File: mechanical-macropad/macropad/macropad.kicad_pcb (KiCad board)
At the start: 2 copper layers, 76 x 176.4 mm, 89 parts, among them J1 USB_B_Micro, J2 AVR-ISP-6, K1 KEYSW, K10 KEYSW, K11 KEYSW, K12 KEYSW, K13 KEYSW, K14 KEYSW, K15 KEYSW, K16 KEYSW, K17 KEYSW, K18 KEYSW, K19 KEYSW, K2 KEYSW, K20 KEYSW, K21 KEYSW, K22 KEYSW, K23 KEYSW, K24 KEYSW, K25 KEYSW, K26 KEYSW, K27 KEYSW, K28 KEYSW, K3 KEYSW, K4 KEYSW, K5 KEYSW, K6 KEYSW, K7 KEYSW, K8 KEYSW, K9 KEYSW, SW1 SW_Push, U1 ATMEGA32U4, X1 XTAL_GND

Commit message: Final cleanup
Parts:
- moved C6 0.59 mm to (175.2, 85.8)
- moved C14 0.28 mm to (159.7, 81.0)
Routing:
- net GND: track 27.7 -> 27.1 mm
- net /ISP_RESET: track 51.7 -> 51.2 mm
- added copper zone on B.Cu, net VCC

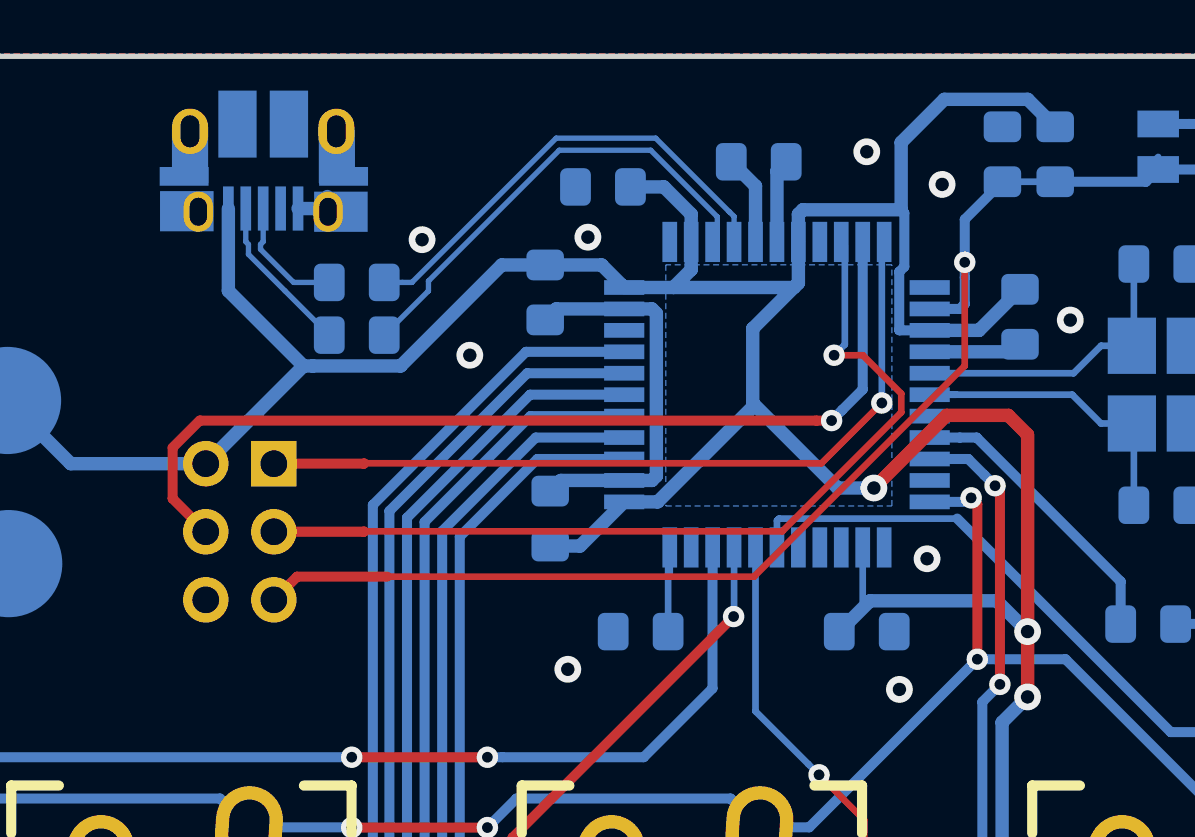
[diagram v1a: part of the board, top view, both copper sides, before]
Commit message: Add a beautiful VCC pour under the MCU to clean up traces
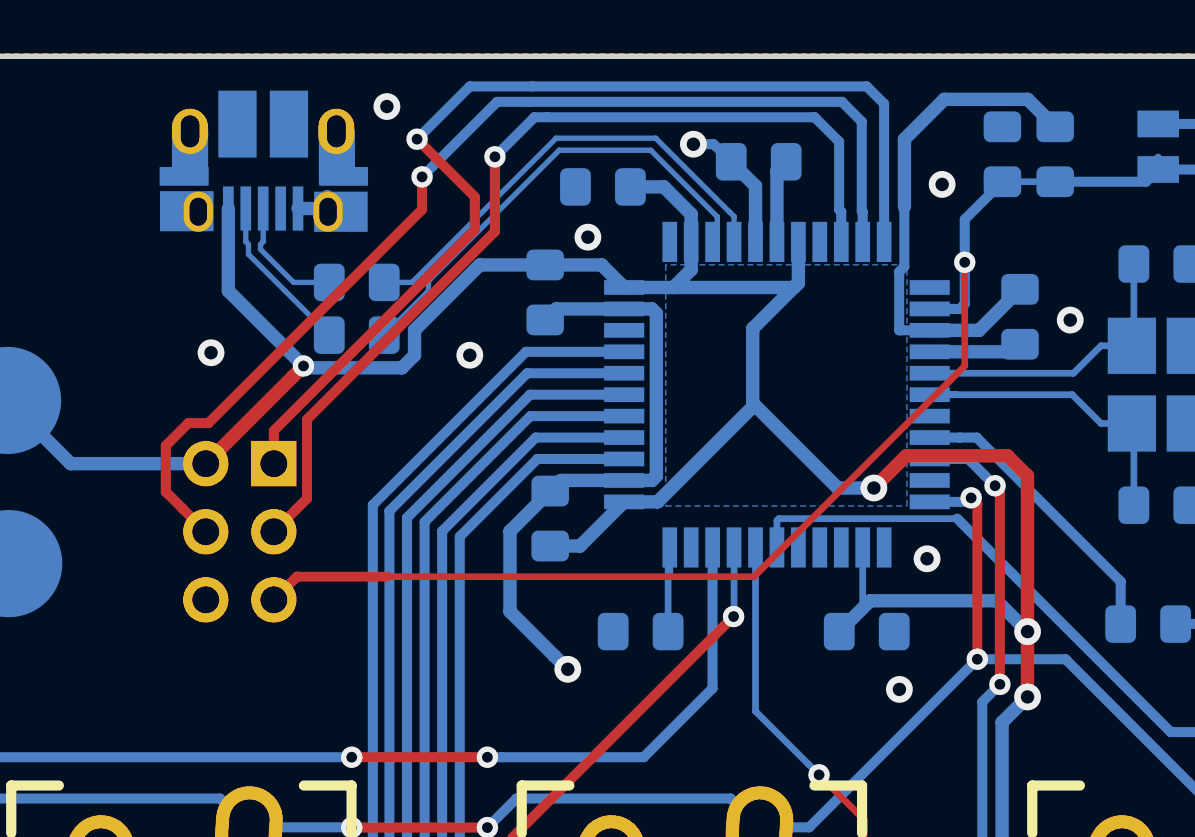
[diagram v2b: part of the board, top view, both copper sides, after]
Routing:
- net /ISP_MISO: track 29.7 -> 39.9 mm
- net GND: track 27.1 -> 36.9 mm, vias 27 -> 28
- net VCC: track 249.7 -> 243.0 mm, vias 4 -> 5
- net /ISP_MOSI: track 35.8 -> 40.6 mm
- net /ISP_SCK: track 33.5 -> 35.0 mm

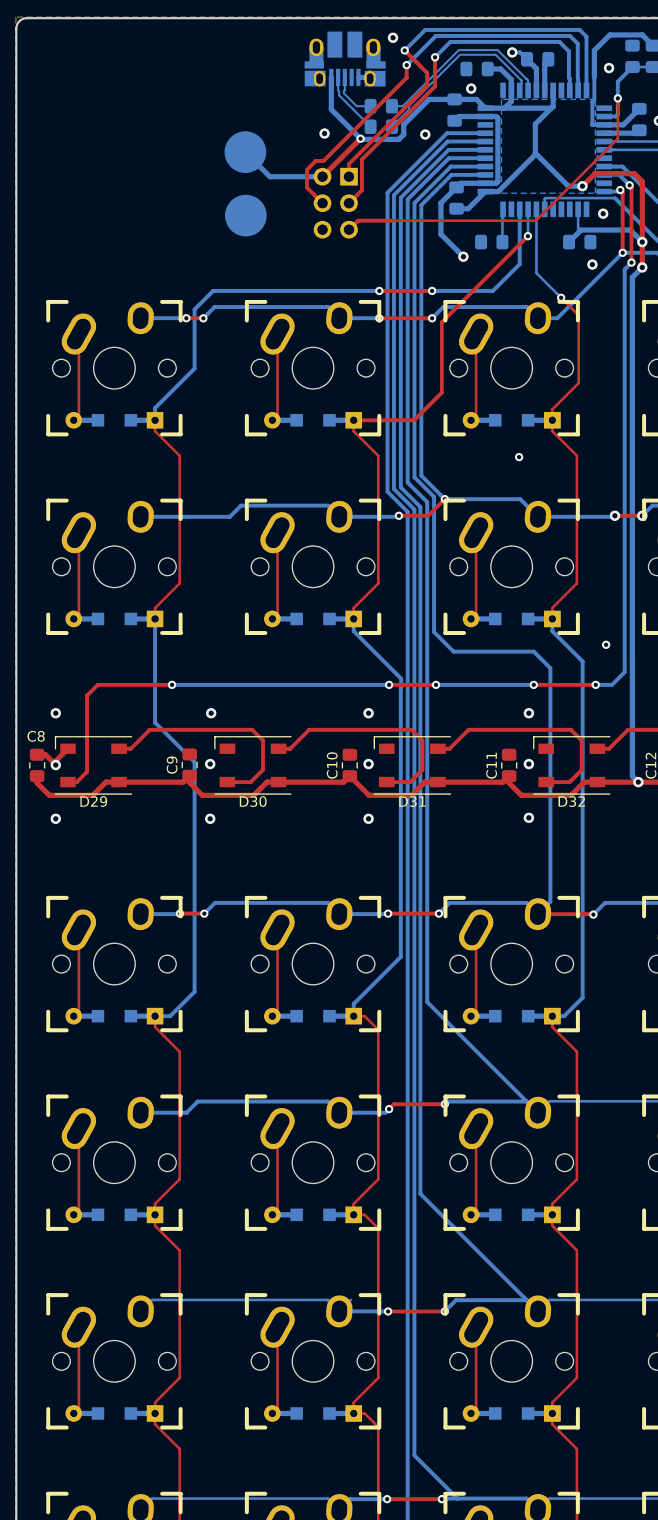
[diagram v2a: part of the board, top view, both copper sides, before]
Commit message: Gild the lily: branding and removal of ugly GND trace
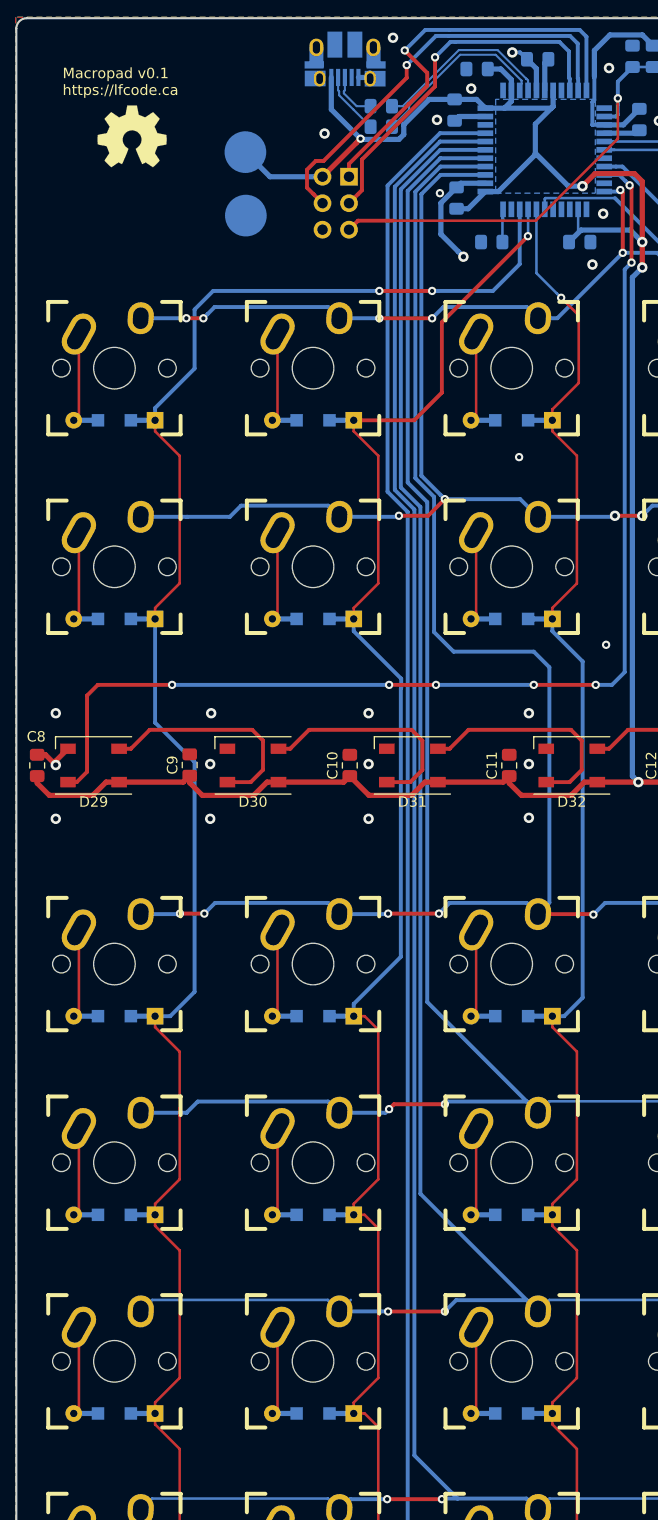
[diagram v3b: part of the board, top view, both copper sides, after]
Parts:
- added REF**: OSHW-Symbol_6.7x6mm_SilkScreen, Symbol:OSHW-Symbol_6.7x6mm_SilkScreen, F.Cu at (126.6, 87.5)
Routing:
- net GND: track 36.9 -> 28.3 mm, vias 28 -> 29
- net Row5: track 183.7 -> 182.7 mm
- net Row4: track 161.7 -> 160.7 mm
- net Row2: track 98.3 -> 99.0 mm
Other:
- board text added: "Macropad v0.1 https://lfcode.ca"

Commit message: Shift to portrait letter paper to make printable
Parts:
- moved C11 65.2 mm to (120.2, 98.4)
- moved D10 65.2 mm to (101.4, 122.4)
- moved D11 65.2 mm to (101.4, 141.5)
- moved D12 65.2 mm to (101.4, 160.5)
- moved D13 65.2 mm to (101.4, 179.6)
- moved D14 65.2 mm to (101.4, 198.6)
- moved D16 65.2 mm to (120.4, 84.3)
- moved D2 65.2 mm to (82.3, 84.3)
- moved D23 65.2 mm to (139.5, 84.3)
- moved D32 65.2 mm to (126.2, 98.4)
- moved D8 65.2 mm to (101.4, 65.3)
- moved D9 65.2 mm to (101.4, 84.3)
- moved K10 65.2 mm to (101.4, 117.4)
- moved K11 65.2 mm to (101.4, 136.5)
- moved K12 65.2 mm to (101.4, 155.5)
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
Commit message: Final touches
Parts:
- removed REF**: OSHW-Symbol_6.7x6mm_SilkScreen, Symbol:OSHW-Symbol_6.7x6mm_SilkScreen
- added H1: MountingHole, MountingHole:MountingHole_3.2mm_M3_Pad, F.Cu at (131.3, 183.3)
- added H2: MountingHole, MountingHole:MountingHole_3.2mm_M3_Pad, F.Cu at (144.4, 37.5)
- added H3: MountingHole, MountingHole:MountingHole_3.2mm_M3_Pad, F.Cu at (93.2, 183.3)
- added H4: MountingHole, MountingHole:MountingHole_3.2mm_M3_Pad, F.Cu at (82.3, 37.5)
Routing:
- net VCC: track 243.0 -> 242.5 mm
- net GND: vias 29 -> 49

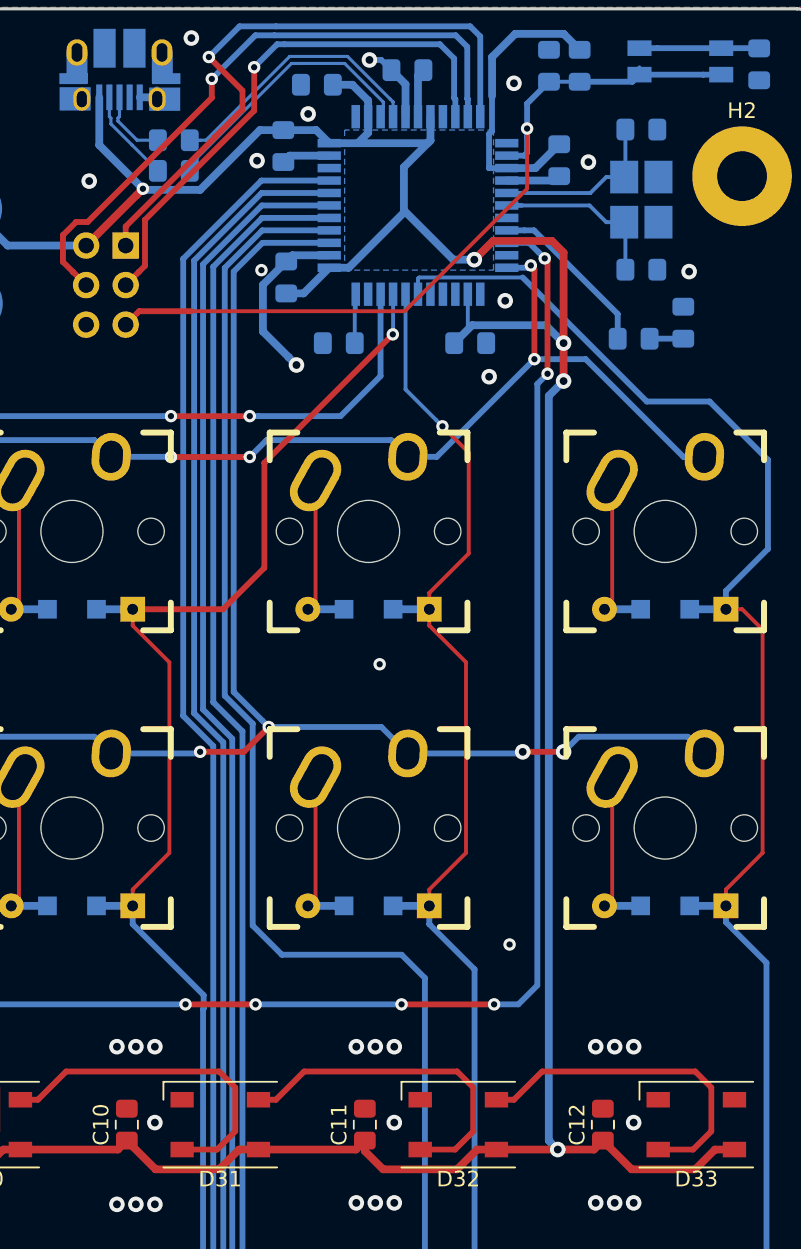
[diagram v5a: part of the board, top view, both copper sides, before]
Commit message: Thicken power traces
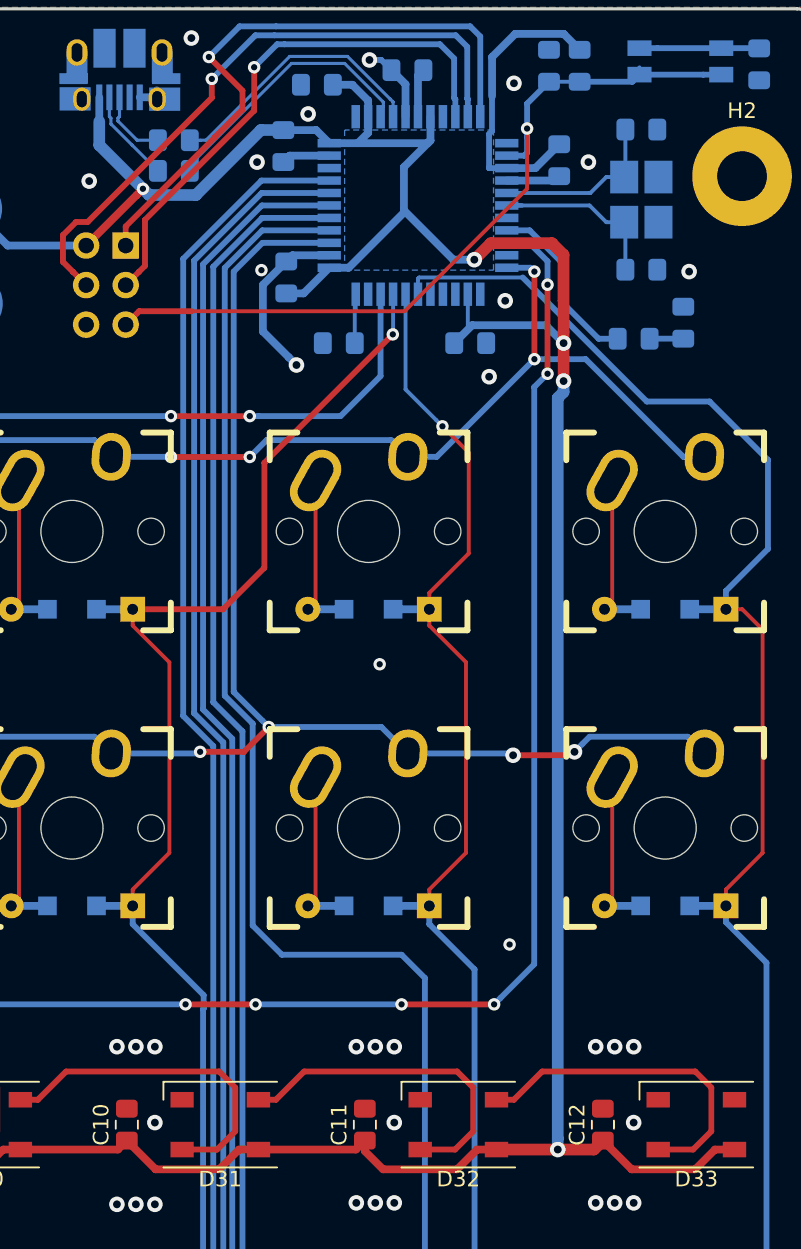
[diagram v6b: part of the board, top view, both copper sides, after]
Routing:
- net /NEOPIXEL_IN: track 111.9 -> 111.0 mm
- net /DBG_LED: track 10.9 -> 11.5 mm
